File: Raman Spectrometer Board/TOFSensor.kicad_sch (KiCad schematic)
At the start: 0 parts

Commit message: TOF sensor
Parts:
- added Conn6: Molex_uF_D_06, MRDT_Connectors:MOLEX_uF_D_06_Horizontal, symbol MRDT_Connectors:Molex_uF_D_06
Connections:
- new net +3V3: Conn6.1, Conn6.6
- new net GND: Conn6.2
- new net GPID: Conn6.5
- new net SCL: Conn6.3
- new net SDA: Conn6.4

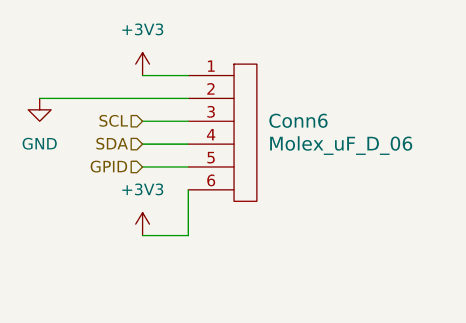
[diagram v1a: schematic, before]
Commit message: tof voltages connected
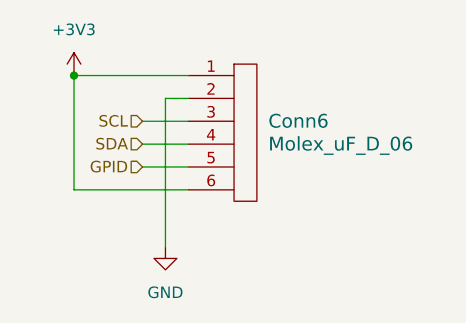
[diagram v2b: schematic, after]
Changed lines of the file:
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@@
 	(generator_version "9.0")
 	(paper "A4")
-	(wire
-		(pts
-			(xy 165.1 77.47) (xy 165.1 82.55)
-		)
-		(stroke
-			(width 0)
-			(type default)
-		)
-	)
-	(wire
-		(pts
-			(xy 148.59 67.31) (xy 165.1 67.31)
-		)
-		(stroke
-			(width 0)
-			(type default)
-		)
-	)
-	(wire
-		(pts
-			(xy 165.1 82.55) (xy 160.02 82.55)
+	(junction
+		(at 152.4 64.77)
+		(diameter 0)
+		(color 0 0 0 0)
+	)
+	(wire
+		(pts
+			(xy 152.4 64.77) (xy 152.4 77.47)
+		)
+		(stroke
+			(width 0)
+			(type default)
+		)
+	)
+	(wire
+		(pts
+			(xy 162.56 83.82) (xy 162.56 67.31)
+		)
+		(stroke
+			(width 0)
+			(type default)
+		)
+	)
+	(wire
+		(pts
+			(xy 162.56 67.31) (xy 165.1 67.31)
+		)
+		(stroke
+			(width 0)
+			(type default)
+		)
+	)
+	(wire
+		(pts
+			(xy 165.1 77.47) (xy 152.4 77.47)
 		)
 		(stroke
@@
 	(wire
 		(pts
-			(xy 160.02 64.77) (xy 165.1 64.77)
+			(xy 152.4 64.77) (xy 165.1 64.77)
 		)
 		(stroke
@@
 	)
 	(symbol
-		(lib_id "power:+3V3")
-		(at 160.02 82.55 0)
-		(unit 1)
-		(exclude_from_sim no)
-		(in_bom yes)
-		(on_board yes)
-		(dnp no)
-		(fields_autoplaced yes)
-		(property "Reference" "#PWR030"
-			(at 160.02 86.36 0)
-			(effects
-				(font
-					(size 1.27 1.27)
-				)
-				(hide yes)
-			)
-		)
-		(property "Value" "+3V3"
-			(at 160.02 77.47 0)
-			(effects
-				(font
-					(size 1.27 1.27)
-				)
-			)
-		)
-		(property "Footprint" ""
-			(at 160.02 82.55 0)
-			(effects
-				(font
-					(size 1.27 1.27)
-				)
-				(hide yes)
-			)
-		)
-		(property "Datasheet" ""
-			(at 160.02 82.55 0)
-			(effects
-				(font
-					(size 1.27 1.27)
-				)
-				(hide yes)
-			)
-		)
-		(property "Description" "Power symbol creates a global label with name \"+3V3\""
-			(at 160.02 82.55 0)
-			(effects
-				(font
-					(size 1.27 1.27)
-				)
-				(hide yes)
-			)
-		)
-		(pin "1"
-		)
-		(instances
-			(project "RamanSpectrometerBoard"
-				(path "/ab487c59-f066-48f5-a383-99e8eaf806bf/57f2af9f-b055-41d8-9bd6-81b53eb984e5"
-					(reference "#PWR030")
-					(unit 1)
-				)
-			)
-		)
-	)
-	(symbol
 		(lib_id "power:GND")
-		(at 148.59 67.31 0)
+		(at 162.56 83.82 0)
 		(unit 1)
 		(exclude_from_sim no)
@@
 		(fields_autoplaced yes)
 		(property "Reference" "#PWR029"
-			(at 148.59 73.66 0)
+			(at 162.56 90.17 0)
 			(effects
 				(font
@@
 		)
 		(property "Value" "GND"
-			(at 148.59 72.39 0)
+			(at 162.56 88.9 0)
 			(effects
 				(font
@@
 		)
 		(property "Footprint" ""
-			(at 148.59 67.31 0)
+			(at 162.56 83.82 0)
 			(effects
 				(font
@@
 		)
 		(property "Datasheet" ""
-			(at 148.59 67.31 0)
+			(at 162.56 83.82 0)
 			(effects
 				(font
@@
 		)
 		(property "Description" "Power symbol creates a global label with name \"GND\" , ground"
-			(at 148.59 67.31 0)
+			(at 162.56 83.82 0)
 			(effects
 				(font
@@
 	(symbol
 		(lib_id "power:+3V3")
-		(at 160.02 64.77 0)
+		(at 152.4 64.77 0)
 		(unit 1)
 		(exclude_from_sim no)
@@
 		(fields_autoplaced yes)
 		(property "Reference" "#PWR028"
-			(at 160.02 68.58 0)
+			(at 152.4 68.58 0)
 			(effects
 				(font
@@
 		)
 		(property "Value" "+3V3"
-			(at 160.02 59.69 0)
+			(at 152.4 59.69 0)
 			(effects
 				(font
@@
 		)
 		(property "Footprint" ""
-			(at 160.02 64.77 0)
+			(at 152.4 64.77 0)
 			(effects
 				(font
@@
 		)
 		(property "Datasheet" ""
-			(at 160.02 64.77 0)
+			(at 152.4 64.77 0)
 			(effects
 				(font
@@
 		)
 		(property "Description" "Power symbol creates a global label with name \"+3V3\""
-			(at 160.02 64.77 0)
-			(effects
-				(font
+			(at 152.4 64.77 0)
+			(effects
+				(font

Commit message: Revert "tof voltages connected"
This reverts commit cb392bf1d60e7f863b02c943ae62205c2a2451bd.
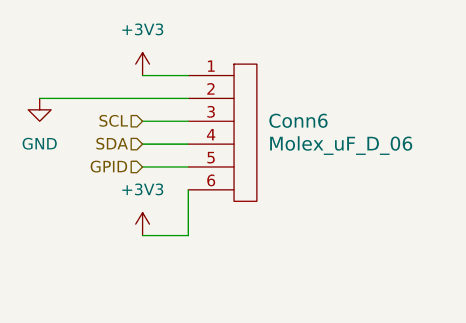
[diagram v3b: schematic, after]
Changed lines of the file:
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@@
 	(generator_version "9.0")
 	(paper "A4")
-	(junction
-		(at 152.4 64.77)
-		(diameter 0)
-		(color 0 0 0 0)
-	)
-	(wire
-		(pts
-			(xy 152.4 64.77) (xy 152.4 77.47)
-		)
-		(stroke
-			(width 0)
-			(type default)
-		)
-	)
-	(wire
-		(pts
-			(xy 162.56 83.82) (xy 162.56 67.31)
-		)
-		(stroke
-			(width 0)
-			(type default)
-		)
-	)
-	(wire
-		(pts
-			(xy 162.56 67.31) (xy 165.1 67.31)
-		)
-		(stroke
-			(width 0)
-			(type default)
-		)
-	)
-	(wire
-		(pts
-			(xy 165.1 77.47) (xy 152.4 77.47)
+	(wire
+		(pts
+			(xy 165.1 77.47) (xy 165.1 82.55)
+		)
+		(stroke
+			(width 0)
+			(type default)
+		)
+	)
+	(wire
+		(pts
+			(xy 148.59 67.31) (xy 165.1 67.31)
+		)
+		(stroke
+			(width 0)
+			(type default)
+		)
+	)
+	(wire
+		(pts
+			(xy 165.1 82.55) (xy 160.02 82.55)
 		)
 		(stroke
@@
 	(wire
 		(pts
-			(xy 152.4 64.77) (xy 165.1 64.77)
+			(xy 160.02 64.77) (xy 165.1 64.77)
 		)
 		(stroke
@@
 	)
 	(symbol
+		(lib_id "power:+3V3")
+		(at 160.02 82.55 0)
+		(unit 1)
+		(exclude_from_sim no)
+		(in_bom yes)
+		(on_board yes)
+		(dnp no)
+		(fields_autoplaced yes)
+		(property "Reference" "#PWR030"
+			(at 160.02 86.36 0)
+			(effects
+				(font
+					(size 1.27 1.27)
+				)
+				(hide yes)
+			)
+		)
+		(property "Value" "+3V3"
+			(at 160.02 77.47 0)
+			(effects
+				(font
+					(size 1.27 1.27)
+				)
+			)
+		)
+		(property "Footprint" ""
+			(at 160.02 82.55 0)
+			(effects
+				(font
+					(size 1.27 1.27)
+				)
+				(hide yes)
+			)
+		)
+		(property "Datasheet" ""
+			(at 160.02 82.55 0)
+			(effects
+				(font
+					(size 1.27 1.27)
+				)
+				(hide yes)
+			)
+		)
+		(property "Description" "Power symbol creates a global label with name \"+3V3\""
+			(at 160.02 82.55 0)
+			(effects
+				(font
+					(size 1.27 1.27)
+				)
+				(hide yes)
+			)
+		)
+		(pin "1"
+		)
+		(instances
+			(project "RamanSpectrometerBoard"
+				(path "/ab487c59-f066-48f5-a383-99e8eaf806bf/57f2af9f-b055-41d8-9bd6-81b53eb984e5"
+					(reference "#PWR030")
+					(unit 1)
+				)
+			)
+		)
+	)
+	(symbol
 		(lib_id "power:GND")
-		(at 162.56 83.82 0)
+		(at 148.59 67.31 0)
 		(unit 1)
 		(exclude_from_sim no)
@@
 		(fields_autoplaced yes)
 		(property "Reference" "#PWR029"
-			(at 162.56 90.17 0)
+			(at 148.59 73.66 0)
 			(effects
 				(font
@@
 		)
 		(property "Value" "GND"
-			(at 162.56 88.9 0)
+			(at 148.59 72.39 0)
 			(effects
 				(font
@@
 		)
 		(property "Footprint" ""
-			(at 162.56 83.82 0)
+			(at 148.59 67.31 0)
 			(effects
 				(font
@@
 		)
 		(property "Datasheet" ""
-			(at 162.56 83.82 0)
+			(at 148.59 67.31 0)
 			(effects
 				(font
@@
 		)
 		(property "Description" "Power symbol creates a global label with name \"GND\" , ground"
-			(at 162.56 83.82 0)
+			(at 148.59 67.31 0)
 			(effects
 				(font
@@
 	(symbol
 		(lib_id "power:+3V3")
-		(at 152.4 64.77 0)
+		(at 160.02 64.77 0)
 		(unit 1)
 		(exclude_from_sim no)
@@
 		(fields_autoplaced yes)
 		(property "Reference" "#PWR028"
-			(at 152.4 68.58 0)
+			(at 160.02 68.58 0)
 			(effects
 				(font
@@
 		)
 		(property "Value" "+3V3"
-			(at 152.4 59.69 0)
+			(at 160.02 59.69 0)
 			(effects
 				(font
@@
 		)
 		(property "Footprint" ""
-			(at 152.4 64.77 0)
+			(at 160.02 64.77 0)
 			(effects
 				(font
@@
 		)
 		(property "Datasheet" ""
-			(at 152.4 64.77 0)
+			(at 160.02 64.77 0)
 			(effects
 				(font
@@
 		)
 		(property "Description" "Power symbol creates a global label with name \"+3V3\""
-			(at 152.4 64.77 0)
-			(effects
-				(font
+			(at 160.02 64.77 0)
+			(effects
+				(font
